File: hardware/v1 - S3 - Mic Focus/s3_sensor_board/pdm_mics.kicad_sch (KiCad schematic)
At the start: 2 parts, among them U501 SHT4x

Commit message: WIP
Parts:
- removed C501: 1uF, Capacitor_SMD:C_0805_2012Metric, symbol Device:C_Small
- removed U501: SHT4x, Sensor_Humidity:Sensirion_DFN-4_1.5x1.5mm_P0.8mm_SHT4x_NoCentralPad, symbol Sensor_Humidity:SHT4x
- added U601: L, BVH_Audio:Knowles_PDM_SMD_ThroughPort, symbol BVH_Audio:Mic_PDM
- added U602: R, BVH_Audio:Knowles_PDM_SMD_ThroughPort, symbol BVH_Audio:Mic_PDM
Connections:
- net +3.3V: now also U601.5 (Vcc), U602.2 (SEL), U602.5 (Vcc)
- net GND: now also U601.2 (SEL), U601.3 (GND), U602.3 (GND)
- new net PDM_CLK: U601.4 (CLK), U602.4 (CLK)
- new net PDM_Din: U601.1 (Dout), U602.1 (Dout)

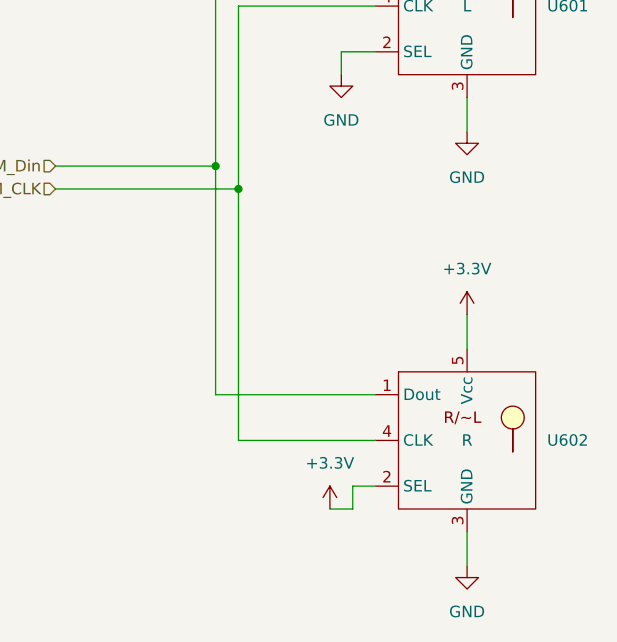
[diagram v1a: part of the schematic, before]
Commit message: Processor placement and routing work
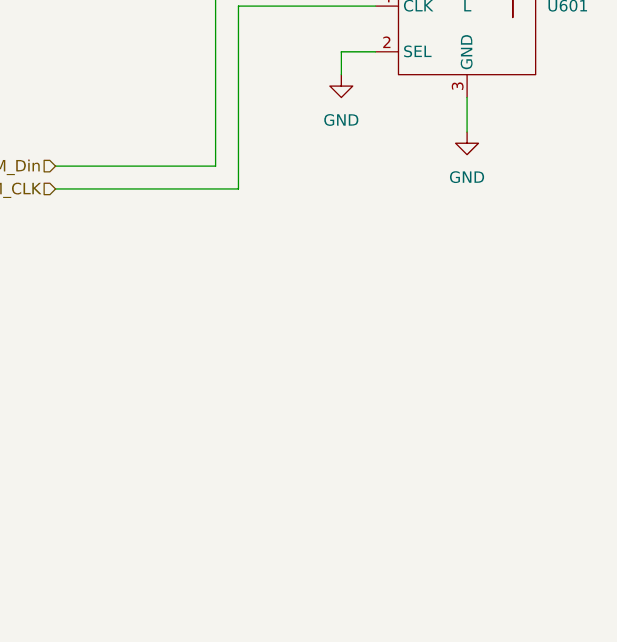
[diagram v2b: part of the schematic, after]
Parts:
- removed U602: R, BVH_Audio:Knowles_PDM_SMD_ThroughPort, symbol BVH_Audio:Mic_PDM

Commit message: WIP
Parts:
- added C601: 0.1uF, Capacitor_SMD:C_0603_1608Metric, symbol Device:C_Small
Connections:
- net +3.3V: now also C601.1
- net GND: now also C601.2
